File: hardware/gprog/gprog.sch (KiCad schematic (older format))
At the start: 23 parts, among them IC1 ATMEGA48P, P1 ISP x2560, P2 USB, P3 ISP x48, U1 74HC126, X1 12MHz

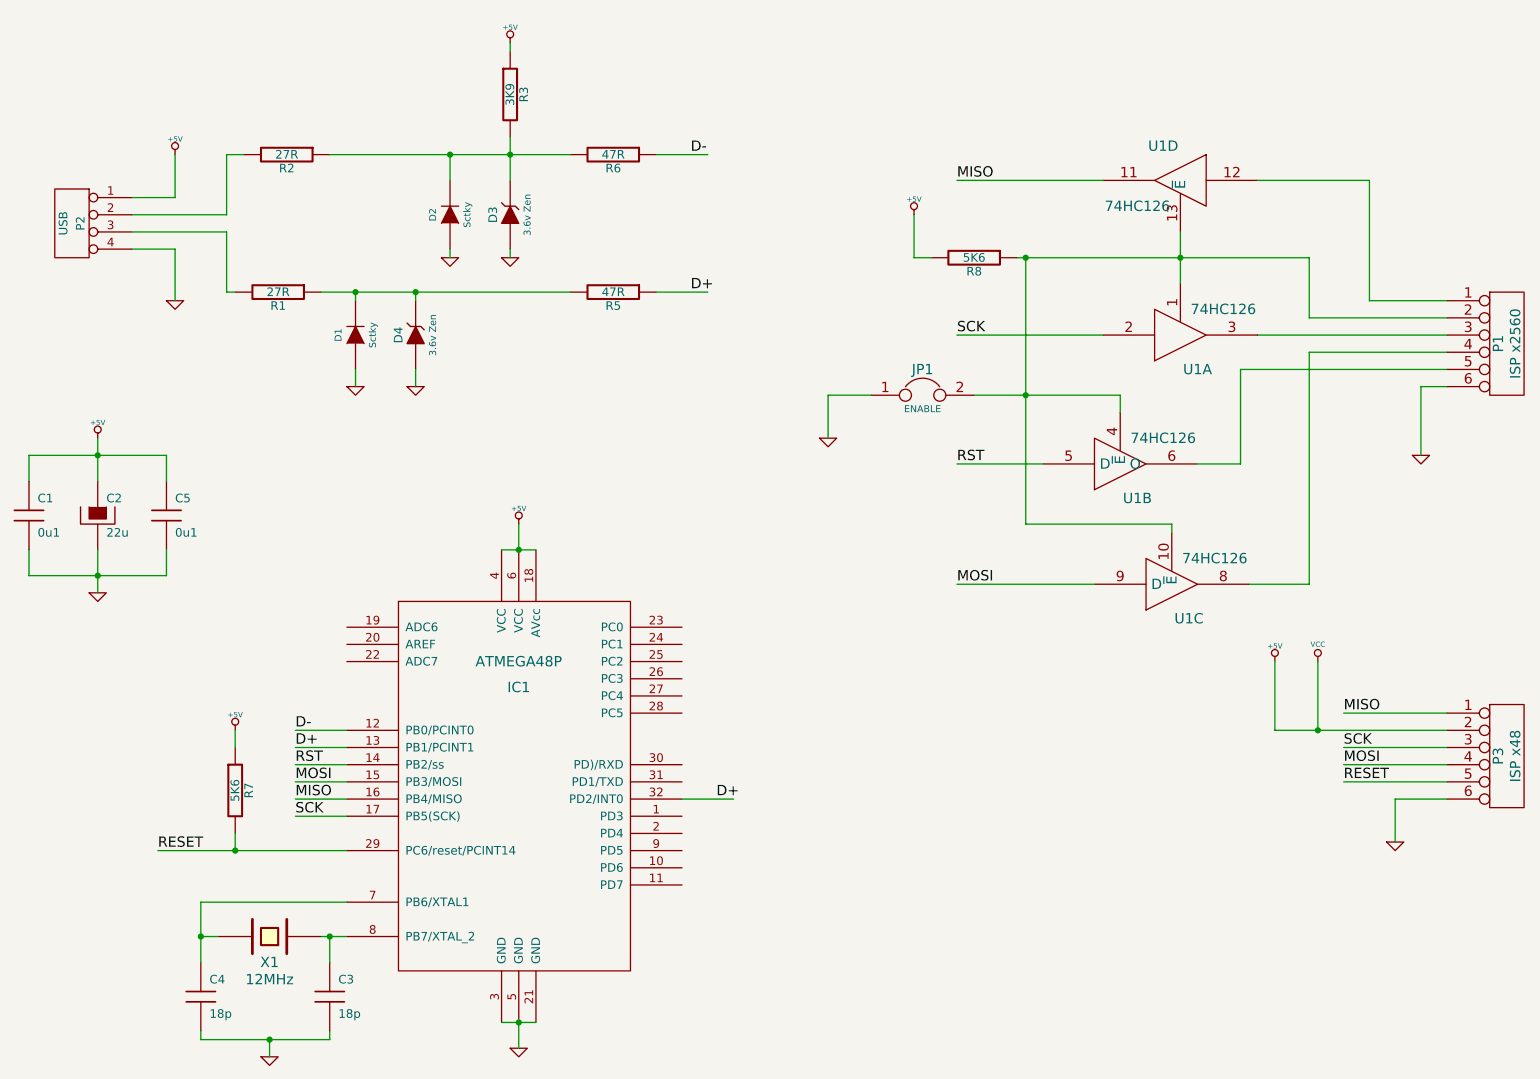
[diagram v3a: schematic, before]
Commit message: gPROG: Fixed errors in schematic. Completed PCB to 'final draft'.
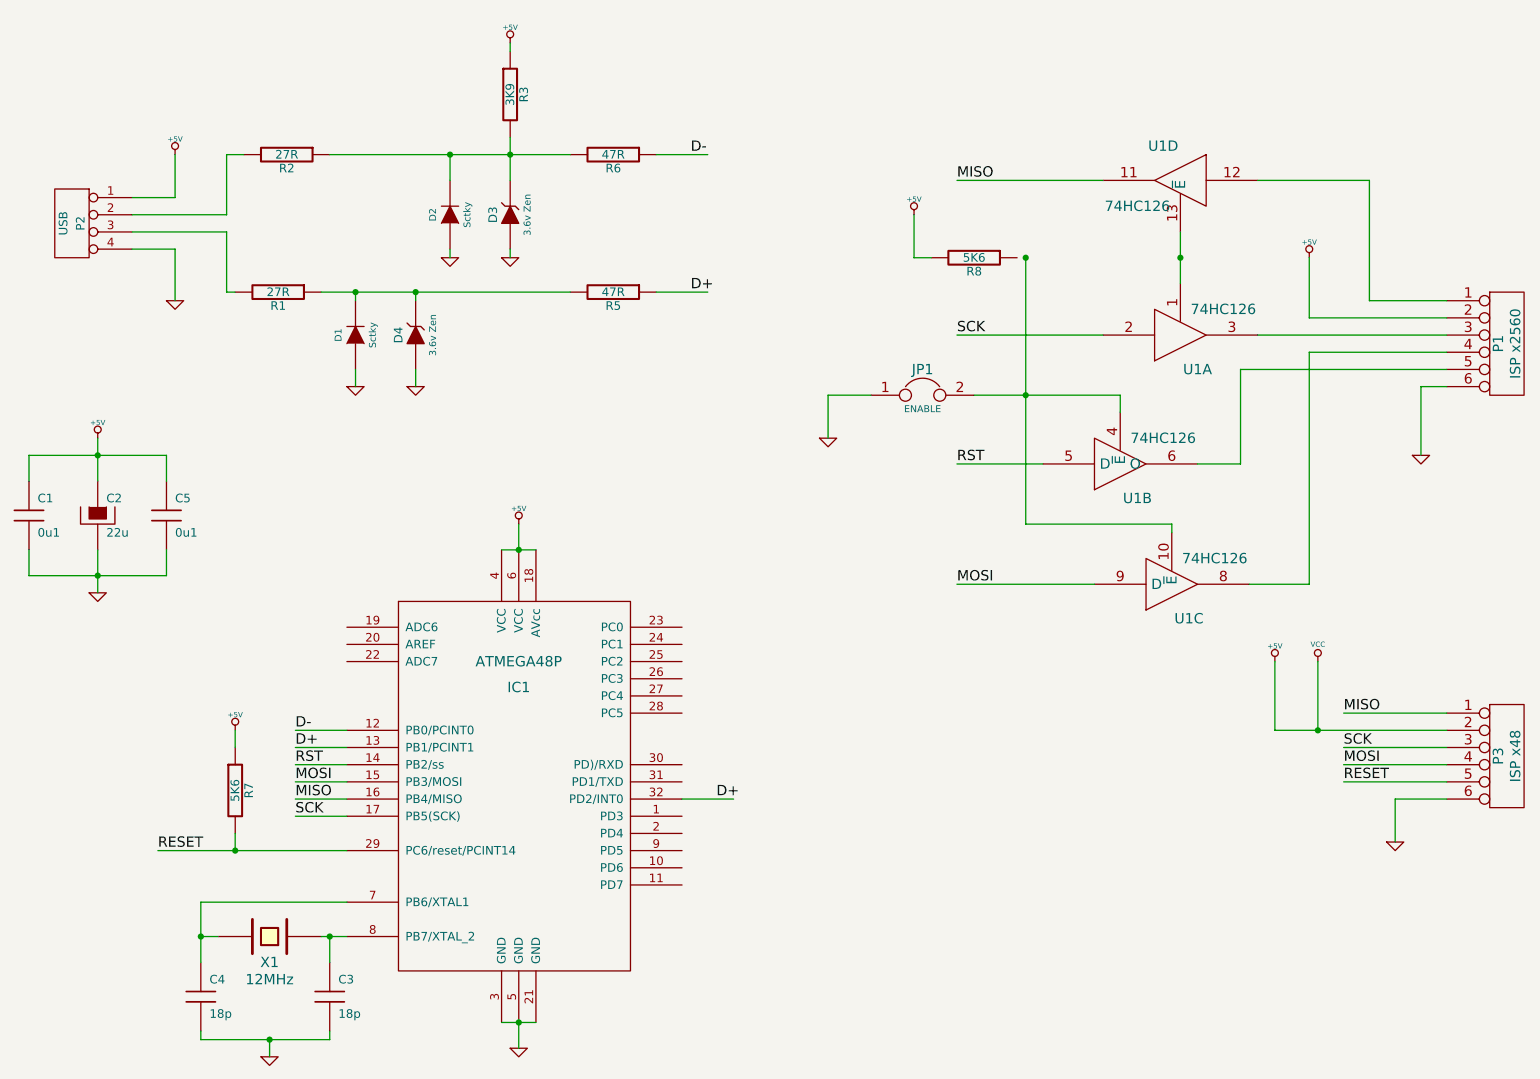
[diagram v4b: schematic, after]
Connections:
- net +5V: now also P1.2
- new net: U1.1, U1.13 (~E)
- new net: JP1.2, U1.10 (~E), U1.4 (~E)
- now unconnected: R8.1
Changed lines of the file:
@@
-EESchema Schematic File Version 2  date 27/11/2011 12:33:56 a.m.
+EESchema Schematic File Version 2  date 27/11/2011 11:14:15 a.m.
 LIBS:power
 LIBS:device
@@
 Comment4 ""
 $EndDescr
+$Comp
+L +5V #PWR?
+U 1 1 4ED164AA
+P 8800 2400
+F 0 "#PWR?" H 8800 2490 20  0001 C CNN
+F 1 "+5V" H 8800 2490 30  0000 C CNN
+	1    8800 2400
+	1    0    0    -1
+$EndComp
 Wire Wire Line
 	8600 5150 8600 4750
 Wire Wire Line
-	6850 3200 7700 3200
+	6850 3200 7150 3200
+Wire Wire Line
+	7150 3200 7700 3200
 Connection ~ 7150 3200
 Wire Wire Line
 	7700 3200 7700 3300
 Wire Wire Line
-	1750 3450 1750 3700
+	1750 3450 1750 3550
+Wire Wire Line
+	1750 3550 1750 3700
 Wire Wire Line
 	2150 3550 2150 3700
 Wire Wire Line
-	2150 3550 1350 3550
+	2150 3550 1750 3550
+Wire Wire Line
+	1750 3550 1350 3550
 Wire Wire Line
 	1350 3550 1350 3700
 Connection ~ 1750 4250
 Wire Wire Line
-	7100 2400 8800 2400
-Wire Wire Line
 	6600 2400 6500 2400
 Wire Wire Line
@@
 	2350 6950 2350 6900
 Wire Wire Line
-	2350 6950 3100 6950
+	2350 6950 2750 6950
+Wire Wire Line
+	2750 6950 3100 6950
 Wire Wire Line
 	3100 6950 3100 6900
 Connection ~ 2350 6350
 Wire Wire Line
-	2350 6500 2350 6150
+	2350 6500 2350 6350
+Wire Wire Line
+	2350 6350 2350 6150
 Wire Wire Line
 	2350 6150 3200 6150
@@
 	2550 5150 2550 5250
 Wire Wire Line
-	2100 5850 3200 5850
+	2100 5850 2550 5850
+Wire Wire Line
+	2550 5850 3200 5850
 Wire Wire Line
 	3200 5250 2900 5250
@@
 Connection ~ 4200 4100
 Wire Wire Line
-	4300 4100 4100 4100
+	4300 4100 4200 4100
+Wire Wire Line
+	4200 4100 4100 4100
 Wire Wire Line
 	9300 5800 9300 5550
@@
 	8800 4300 8450 4300
 Wire Wire Line
-	8050 2250 8050 2550
+	8050 2250 8050 2400
+Wire Wire Line
+	8050 2400 8050 2550
 Wire Wire Line
 	8800 2400 8800 2750
@@
 	2600 1800 2500 1800
 Wire Wire Line
-	4500 1800 3100 1800
+	4500 1800 4150 1800
+Wire Wire Line
+	4150 1800 3800 1800
+Wire Wire Line
+	3800 1800 3100 1800
 Wire Wire Line
 	4150 1200 4150 1150
@@
 	3800 2350 3800 2400
 Wire Wire Line
-	3050 2600 4500 2600
+	3050 2600 3250 2600
+Wire Wire Line
+	3250 2600 3600 2600
+Wire Wire Line
+	3600 2600 4500 2600
 Wire Wire Line
 	3250 2600 3250 2650
@@
 	5000 1800 5300 1800
 Wire Wire Line
-	4150 1950 4150 1700
+	4150 1950 4150 1800
+Wire Wire Line
+	4150 1800 4150 1700
 Wire Wire Line
 	2550 2600 2500 2600
@@
 	7600 1950 6750 1950
 Wire Wire Line
-	9600 5150 8600 5150
+	9600 5150 8850 5150
+Wire Wire Line
+	8850 5150 8600 5150
 Wire Wire Line
 	9600 5350 9000 5350
@@
 	4200 3950 4200 4100
 Wire Wire Line
-	4300 6850 4100 6850
+	4300 6850 4200 6850
+Wire Wire Line
+	4200 6850 4100 6850
 Connection ~ 4200 6850
 Wire Wire Line
@@
 Connection ~ 2550 5850
 Wire Wire Line
-	3200 6350 3050 6350
+	3200 6350 3100 6350
+Wire Wire Line
+	3100 6350 3050 6350
 Wire Wire Line
 	2450 6350 2350 6350
@@
 	2150 4250 2150 4100
 Wire Wire Line
-	2150 4250 1350 4250
+	2150 4250 1750 4250
+Wire Wire Line
+	1750 4250 1350 4250
 Wire Wire Line
 	1350 4250 1350 4100
 Wire Wire Line
-	1750 4350 1750 4100
+	1750 4350 1750 4250
+Wire Wire Line
+	1750 4250 1750 4100
 Connection ~ 1750 3550
 Wire Wire Line
@@
 	7150 3950 8000 3950
 Wire Wire Line
-	7150 2400 7150 3950
+	7150 2400 7150 3200
+Wire Wire Line
+	7150 3200 7150 3950
 Connection ~ 7150 2400
 Wire Wire Line

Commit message: gPROG: Tidied up PCB some more. Schematic had not been saved prior to previous commits. :-/
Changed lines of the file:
@@
-EESchema Schematic File Version 2  date 27/11/2011 11:14:15 a.m.
+EESchema Schematic File Version 2  date 27/11/2011 12:21:00 p.m.
 LIBS:power
 LIBS:device
@@
 $EndDescr
 $Comp
-L +5V #PWR?
+L +5V #PWR01
 U 1 1 4ED164AA
 P 8800 2400
-F 0 "#PWR?" H 8800 2490 20  0001 C CNN
+F 0 "#PWR01" H 8800 2490 20  0001 C CNN
 F 1 "+5V" H 8800 2490 30  0000 C CNN
 	1    8800 2400
@@
 	8600 5150 8600 4750
 Wire Wire Line
-	6850 3200 7150 3200
-Wire Wire Line
-	7150 3200 7700 3200
+	6850 3200 7700 3200
 Connection ~ 7150 3200
 Wire Wire Line
 	7700 3200 7700 3300
 Wire Wire Line
-	1750 3450 1750 3550
-Wire Wire Line
-	1750 3550 1750 3700
+	1750 3450 1750 3700
 Wire Wire Line
 	2150 3550 2150 3700
 Wire Wire Line
-	2150 3550 1750 3550
-Wire Wire Line
-	1750 3550 1350 3550
+	2150 3550 1350 3550
 Wire Wire Line
 	1350 3550 1350 3700
@@
 	2350 6950 2350 6900
 Wire Wire Line
-	2350 6950 2750 6950
-Wire Wire Line
-	2750 6950 3100 6950
+	2350 6950 3100 6950
 Wire Wire Line
 	3100 6950 3100 6900
 Connection ~ 2350 6350
 Wire Wire Line
-	2350 6500 2350 6350
-Wire Wire Line
-	2350 6350 2350 6150
+	2350 6500 2350 6150
 Wire Wire Line
 	2350 6150 3200 6150
@@
 	2550 5150 2550 5250
 Wire Wire Line
-	2100 5850 2550 5850
-Wire Wire Line
-	2550 5850 3200 5850
+	2100 5850 3200 5850
 Wire Wire Line
 	3200 5250 2900 5250
@@
 Connection ~ 4200 4100
 Wire Wire Line
-	4300 4100 4200 4100
-Wire Wire Line
-	4200 4100 4100 4100
+	4300 4100 4100 4100
 Wire Wire Line
 	9300 5800 9300 5550
@@
 	8800 4300 8450 4300
 Wire Wire Line
-	8050 2250 8050 2400
-Wire Wire Line
-	8050 2400 8050 2550
+	8050 2250 8050 2550
 Wire Wire Line
 	8800 2400 8800 2750
@@
 	2600 1800 2500 1800
 Wire Wire Line
-	4500 1800 4150 1800
-Wire Wire Line
-	4150 1800 3800 1800
-Wire Wire Line
-	3800 1800 3100 1800
+	4500 1800 3100 1800
 Wire Wire Line
 	4150 1200 4150 1150
@@
 	3800 2350 3800 2400
 Wire Wire Line
-	3050 2600 3250 2600
-Wire Wire Line
-	3250 2600 3600 2600
-Wire Wire Line
-	3600 2600 4500 2600
+	3050 2600 4500 2600
 Wire Wire Line
 	3250 2600 3250 2650
@@
 	5000 1800 5300 1800
 Wire Wire Line
-	4150 1950 4150 1800
-Wire Wire Line
-	4150 1800 4150 1700
+	4150 1950 4150 1700
 Wire Wire Line
 	2550 2600 2500 2600
@@
 	7600 1950 6750 1950
 Wire Wire Line
-	9600 5150 8850 5150
-Wire Wire Line
-	8850 5150 8600 5150
+	9600 5150 8600 5150
 Wire Wire Line
 	9600 5350 9000 5350
@@
 	4200 3950 4200 4100
 Wire Wire Line
-	4300 6850 4200 6850
-Wire Wire Line
-	4200 6850 4100 6850
+	4300 6850 4100 6850
 Connection ~ 4200 6850
 Wire Wire Line
@@
 Connection ~ 2550 5850
 Wire Wire Line
-	3200 6350 3100 6350
-Wire Wire Line
-	3100 6350 3050 6350
+	3200 6350 3050 6350
 Wire Wire Line
 	2450 6350 2350 6350
@@
 	2150 4250 2150 4100
 Wire Wire Line
-	2150 4250 1750 4250
-Wire Wire Line
-	1750 4250 1350 4250
+	2150 4250 1350 4250
 Wire Wire Line
 	1350 4250 1350 4100
 Wire Wire Line
-	1750 4350 1750 4250
-Wire Wire Line
-	1750 4250 1750 4100
+	1750 4350 1750 4100
 Connection ~ 1750 3550
 Wire Wire Line
@@
 	7150 3950 8000 3950
 Wire Wire Line
-	7150 2400 7150 3200
-Wire Wire Line
-	7150 3200 7150 3950
+	7150 2400 7150 3950
 Connection ~ 7150 2400
 Wire Wire Line
@@
 Connection ~ 8850 5150
 $Comp
-L VCC #PWR01
+L VCC #PWR02
 U 1 1 4ED0B44E
 P 8850 4750
-F 0 "#PWR01" H 8850 4850 30  0001 C CNN
+F 0 "#PWR02" H 8850 4850 30  0001 C CNN
 F 1 "VCC" H 8850 4850 30  0000 C CNN
 	1    8850 4750
@@
 $EndComp
 $Comp
-L GND #PWR02
+L GND #PWR03
 U 1 1 4ED0AC2D
 P 6000 3450
-F 0 "#PWR02" H 6000 3450 30  0001 C CNN
+F 0 "#PWR03" H 6000 3450 30  0001 C CNN
 F 1 "GND" H 6000 3380 30  0001 C CNN
 	1    6000 3450
@@
 $EndComp
 $Comp
-L +5V #PWR03
+L +5V #PWR04
 U 1 1 4ED08824
 P 1750 3450
-F 0 "#PWR03" H 1750 3540 20  0001 C CNN
+F 0 "#PWR04" H 1750 3540 20  0001 C CNN
 F 1 "+5V" H 1750 3540 30  0000 C CNN
 	1    1750 3450
@@
 $EndComp
 $Comp
-L GND #PWR04
+L GND #PWR05
 U 1 1 4ED08810
 P 1750 4350
-F 0 "#PWR04" H 1750 4350 30  0001 C CNN
+F 0 "#PWR05" H 1750 4350 30  0001 C CNN
 F 1 "GND" H 1750 4280 30  0001 C CNN
 	1    1750 4350
@@
 D+
 $Comp
-L GND #PWR05
+L GND #PWR06
 U 1 1 4ECC4B90
 P 2750 7050
-F 0 "#PWR05" H 2750 7050 30  0001 C CNN
+F 0 "#PWR06" H 2750 7050 30  0001 C CNN
 F 1 "GND" H 2750 6980 30  0001 C CNN
 	1    2750 7050
@@
 $EndComp
 $Comp
-L +5V #PWR06
+L +5V #PWR07
 U 1 1 4ECC4A1D
 P 2550 5150
-F 0 "#PWR06" H 2550 5240 20  0001 C CNN
+F 0 "#PWR07" H 2550 5240 20  0001 C CNN
 F 1 "+5V" H 2550 5240 30  0000 C CNN
 	1    2550 5150
@@
 D-
 $Comp
-L GND #PWR07
+L GND #PWR08
 U 1 1 4ECC4963
 P 4200 7000
-F 0 "#PWR07" H 4200 7000 30  0001 C CNN
+F 0 "#PWR08" H 4200 7000 30  0001 C CNN
 F 1 "GND" H 4200 6930 30  0001 C CNN
 	1    4200 7000
@@
 $EndComp
 $Comp
-L +5V #PWR08
+L +5V #PWR09
 U 1 1 4ECC494B
 P 4200 3950
-F 0 "#PWR08" H 4200 4040 20  0001 C CNN
+F 0 "#PWR09" H 4200 4040 20  0001 C CNN
 F 1 "+5V" H 4200 4040 30  0000 C CNN
 	1    4200 3950
@@
 MISO
 $Comp
-L +5V #VCC09
+L +5V #VCC010
 U 1 1 4ECB2F25
 P 8600 4750
-F 0 "#VCC09" H 8600 4840 20  0001 C CNN
+F 0 "#VCC010" H 8600 4840 20  0001 C CNN
 F 1 "+5V" H 8600 4840 30  0000 C CNN
 	1    8600 4750
@@
 $EndComp
 $Comp
-L GND #PWR010
+L GND #PWR011
 U 1 1 4ECB2F15
 P 9300 5800
-F 0 "#PWR010" H 9300 5800 30  0001 C CNN
+F 0 "#PWR011" H 9300 5800 30  0001 C CNN
 F 1 "GND" H 9300 5730 30  0001 C CNN
 	1    9300 5800
@@
 MISO
 $Comp
-L GND #PWR011
+L GND #PWR012
 U 1 1 4ECB2CC4
 P 9450 3550
-F 0 "#PWR011" H 9450 3550 30  0001 C CNN
+F 0 "#PWR012" H 9450 3550 30  0001 C CNN
 F 1 "GND" H 9450 3480 30  0001 C CNN
 	1    9450 3550
@@
 $EndComp
 $Comp
-L +5V #PWR012
+L +5V #PWR013
 U 1 1 4ECB2C7C
 P 6500 2150
-F 0 "#PWR012" H 6500 2240 20  0001 C CNN
+F 0 "#PWR013" H 6500 2240 20  0001 C CNN
 F 1 "+5V" H 6500 2240 30  0000 C CNN
 	1    6500 2150
@@
 D-
 $Comp
-L +5V #PWR013
+L +5V #PWR014
 U 1 1 4E912AAE
 P 4150 1150
-F 0 "#PWR013" H 4150 1240 20  0001 C CNN
+F 0 "#PWR014" H 4150 1240 20  0001 C CNN
 F 1 "+5V" H 4150 1240 30  0000 C CNN
 	1    4150 1150
@@
 $EndComp
 $Comp
-L GND #PWR014
+L GND #PWR015
 U 1 1 4E912A17
 P 4150 2400
-F 0 "#PWR014" H 4150 2400 30  0001 C CNN
+F 0 "#PWR015" H 4150 2400 30  0001 C CNN
 F 1 "GND" H 4150 2330 30  0001 C CNN
 	1    4150 2400
@@
 $EndComp
 $Comp
-L GND #PWR015
+L GND #PWR016
 U 1 1 4E912A11
 P 3800 2400
-F 0 "#PWR015" H 3800 2400 30  0001 C CNN
+F 0 "#PWR016" H 3800 2400 30  0001 C CNN
 F 1 "GND" H 3800 2330 30  0001 C CNN
 	1    3800 2400
@@
 $EndComp
 $Comp
-L GND #PWR016
+L GND #PWR017
 U 1 1 4E912A0A
 P 3600 3150
-F 0 "#PWR016" H 3600 3150 30  0001 C CNN
+F 0 "#PWR017" H 3600 3150 30  0001 C CNN
 F 1 "GND" H 3600 3080 30  0001 C CNN
 	1    3600 3150
@@
 $EndComp
 $Comp
-L GND #PWR017
+L GND #PWR018
 U 1 1 4E912A03
 P 3250 3150
-F 0 "#PWR017" H 3250 3150 30  0001 C CNN
+F 0 "#PWR018" H 3250 3150 30  0001 C CNN
 F 1 "GND" H 3250 3080 30  0001 C CNN
 	1    3250 3150
@@
 $EndComp
 $Comp
-L GND #PWR018
+L GND #PWR019
 U 1 1 4E91292A
 P 2200 2650
-F 0 "#PWR018" H 2200 2650 30  0001 C CNN
+F 0 "#PWR019" H 2200 2650 30  0001 C CNN
 F 1 "GND" H 2200 2580 30  0001 C CNN
 	1    2200 2650
@@
 $EndComp
 $Comp
-L +5V #PWR019
+L +5V #PWR020
 U 1 1 4E91291D
 P 2200 1800
-F 0 "#PWR019" H 2200 1890 20  0001 C CNN
+F 0 "#PWR020" H 2200 1890 20  0001 C CNN
 F 1 "+5V" H 2200 1890 30  0000 C CNN
 	1    2200 1800
